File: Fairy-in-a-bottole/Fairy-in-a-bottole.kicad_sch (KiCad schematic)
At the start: 28 parts, among them J1 FTDI, Q1 2N7000, U1 ESP32-WROOM-32D, U2 AMS1117-3.3, U3 BL8573CB6TR, U4 FS8205A, U5 DW01A, U6 SLM2169

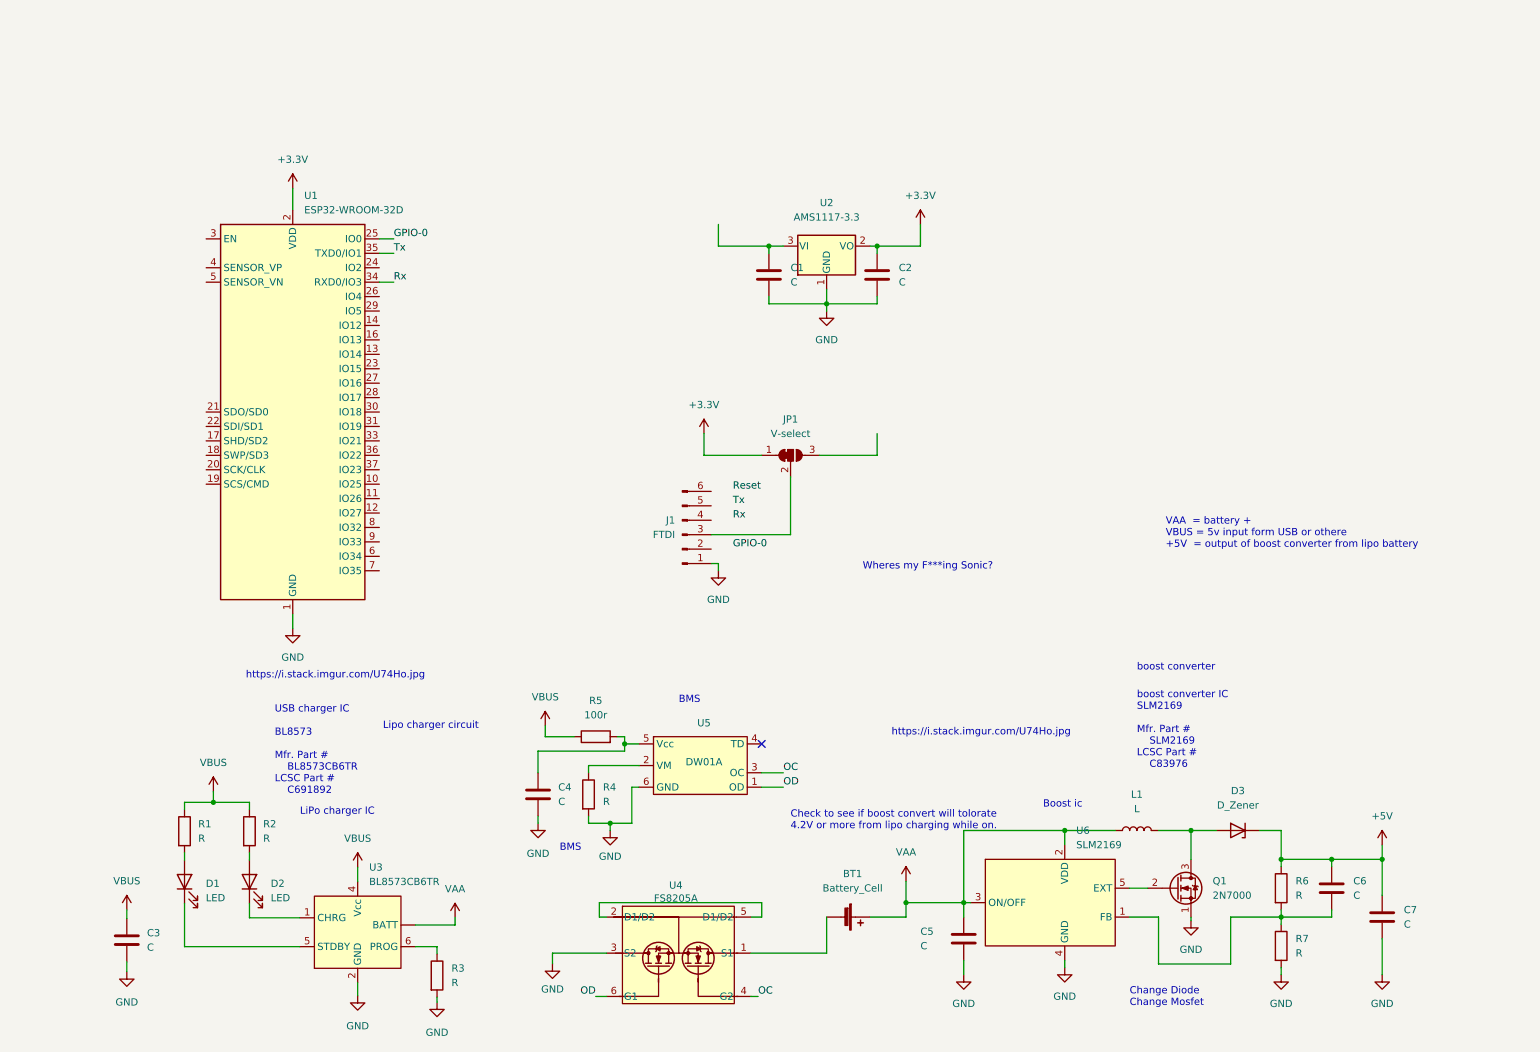
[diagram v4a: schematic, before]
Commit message: added MPTT part and some footprints, and comments
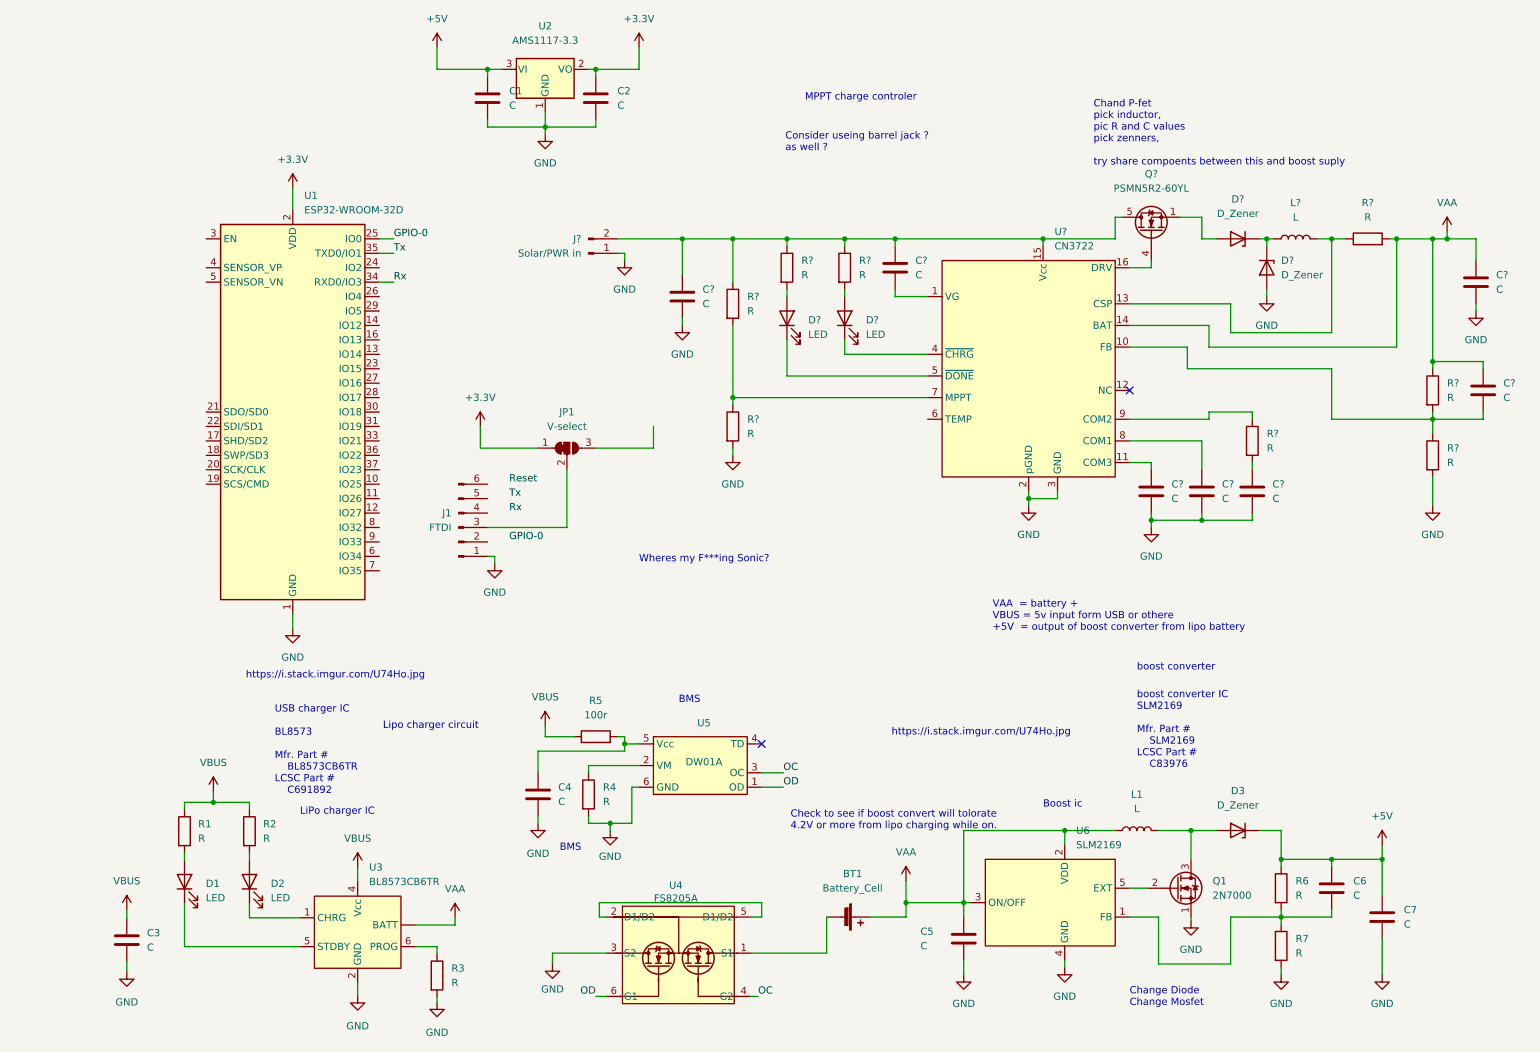
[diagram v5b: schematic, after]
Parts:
- added C? (x7): C, Capacitor_SMD:C_0805_2012Metric_Pad1.18x1.45mm_HandSolder, symbol Device:C
- added D? (x2): D_Zener, Diode_SMD:D_1210_3225Metric, symbol Device:D_Zener
- added D? (x2): LED, Diode_SMD:D_3220_8050Metric_Pad2.65x5.15mm_HandSolder, symbol Device:LED
- added J?: Solar/PWR in, Connector_PinSocket_2.54mm:PinSocket_1x02_P2.54mm_Vertical, symbol Connector:Conn_01x02_Male
- added L?: L, Inductor_SMD:L_12x12mm_H8mm, symbol Device:L
- added Q?: PSMN5R2-60YL, Package_TO_SOT_SMD:LFPAK56, symbol Transistor_FET:PSMN5R2-60YL
- added R? (x8): R, Resistor_SMD:R_0603_1608Metric, symbol Device:R
- added U?: CN3722, Package_SO:TSSOP-16_4.4x5mm_P0.65mm, symbol LIPO-things:CN3722
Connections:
- net +5V: now also C1.1, U2.3 (VI)
- net GND: now also C?.2, C?.2, C?.2, C?.2, C?.2, D?.2 (A), J?.1 (Pin_1), R?.2, R?.2, U?.2 (pGND), U?.3 (GND)
- net VAA: now also C?.1, C?.1, R?.1, R?.2, U?.14 (BAT)
- new net: D?.1 (K), D?.1 (K), L?.1
- new net: D?.2 (A), Q?.1 (S), Q?.2 (S), Q?.3 (S)
- new net: C?.1, C?.1, J?.2 (Pin_2), Q?.5 (D), R?.1, R?.1, R?.1, U?.15 (Vcc)
- new net: R?.1, R?.2, U?.7 (MPPT)
- new net: C?.2, U?.1 (VG)
- new net: C?.2, R?.1, R?.2, U?.10 (FB)
- new net: C?.1, U?.8 (COM1)
- new net: C?.1, R?.2
- new net: R?.1, U?.9 (COM2)
- new net: C?.1, U?.11 (COM3)
- new net: L?.2, R?.1, U?.13 (CSP)
- new net: Q?.4 (G), U?.16 (DRV)
- new net: D?.1 (K), U?.4 (~{CHRG})
- new net: D?.1 (K), U?.5 (~{DONE})
- new net: D?.2 (A), R?.2 (x2)
- no-connect marks 1 -> 2
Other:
- note added: "Chand P-fet pick inductor, pic R and C values pick zenners, try share compoents between this and boost suply"
- note added: "Consider useing barrel jack ? as well ?"
- note added: "MPPT charge controler"
- moved on the sheet: C1, C2, J1, JP1, U2

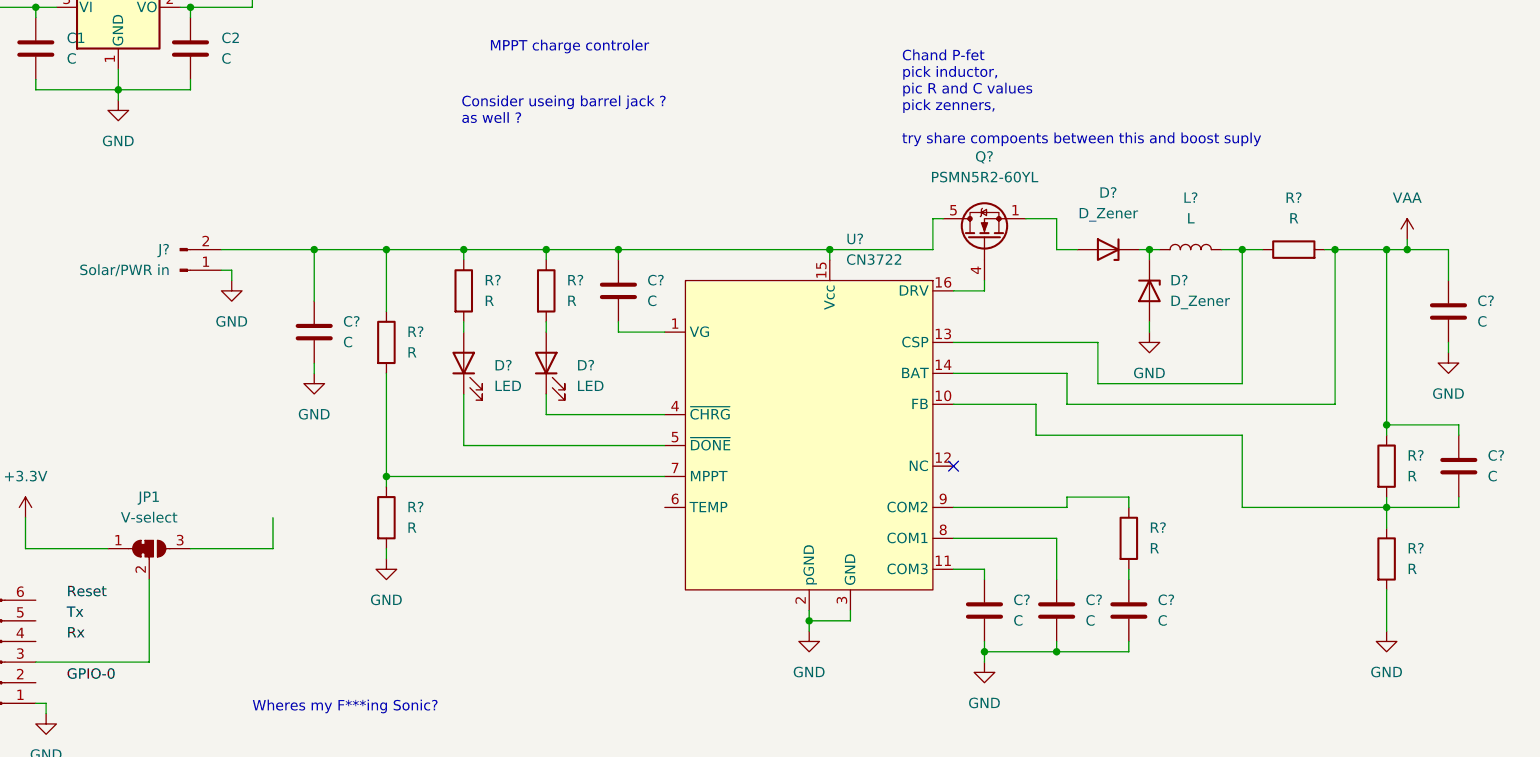
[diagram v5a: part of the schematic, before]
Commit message: asigned foorprints and populated the pcb with them
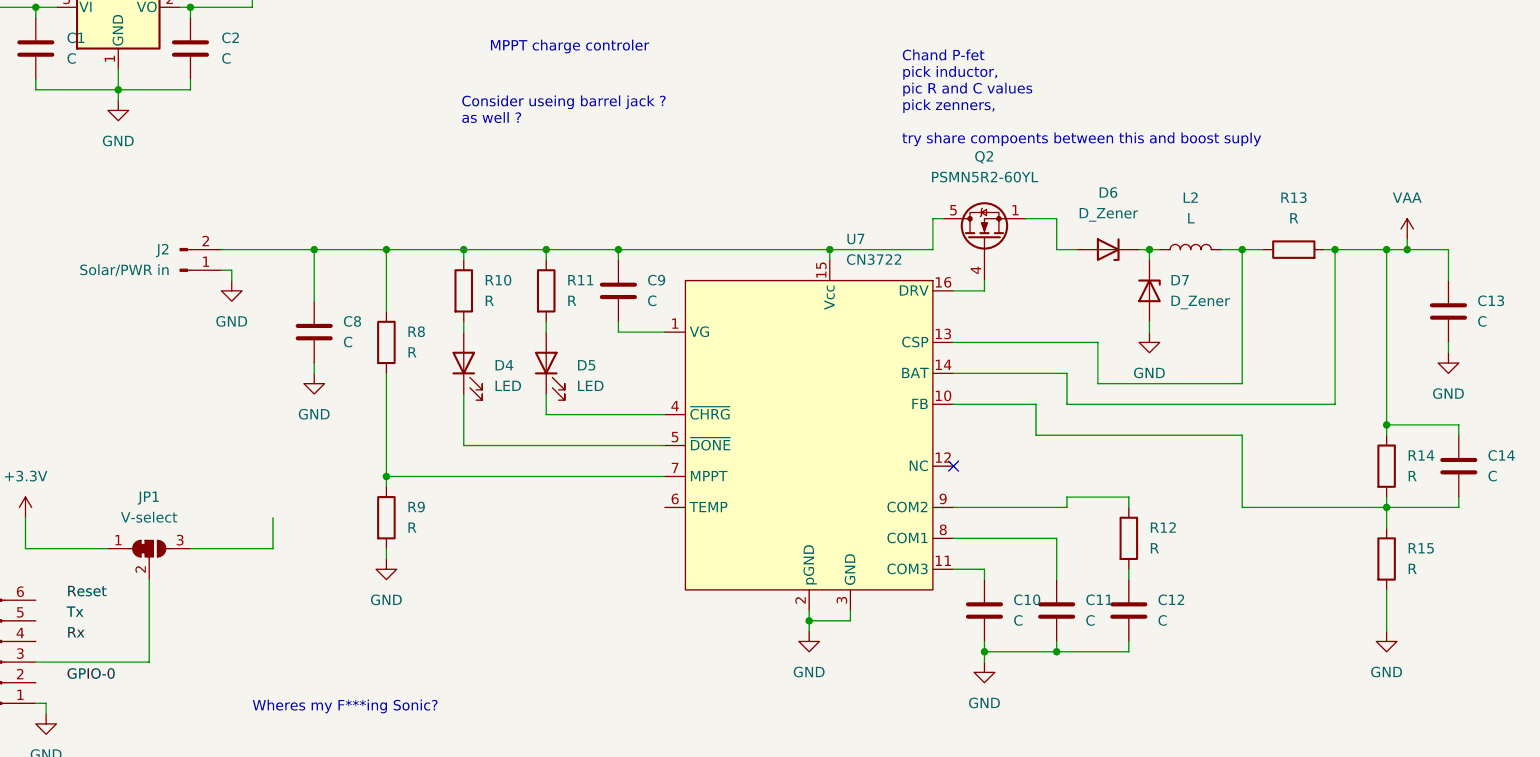
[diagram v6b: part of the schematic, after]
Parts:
- gave numbers to parts that had none: 23

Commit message: just adding some notes
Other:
- note added: "Simba did nothing wrong!"
- note added: "for charging, suguestu using IP2312 (switching)"
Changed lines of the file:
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@@
+    (effects (font (size 1.27 1.27)) (justify left bottom))
+  )
+  (text "for charging, suguestu using \nIP2312 (switching) " (at 101.6 130.81 0)
     (effects (font (size 1.27 1.27)) (justify left bottom))
   )
@@
     (effects (font (size 1.27 1.27)) (justify left bottom))
   )
+  (text "Simba did nothing wrong!" (at 138.43 114.3 0)
+    (effects (font (size 1.27 1.27)) (justify left bottom))
+  )
